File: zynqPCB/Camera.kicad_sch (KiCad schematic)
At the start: 14 parts, among them J4 HDMI_A, U19 PCA9306, U20 xc7z020clg484

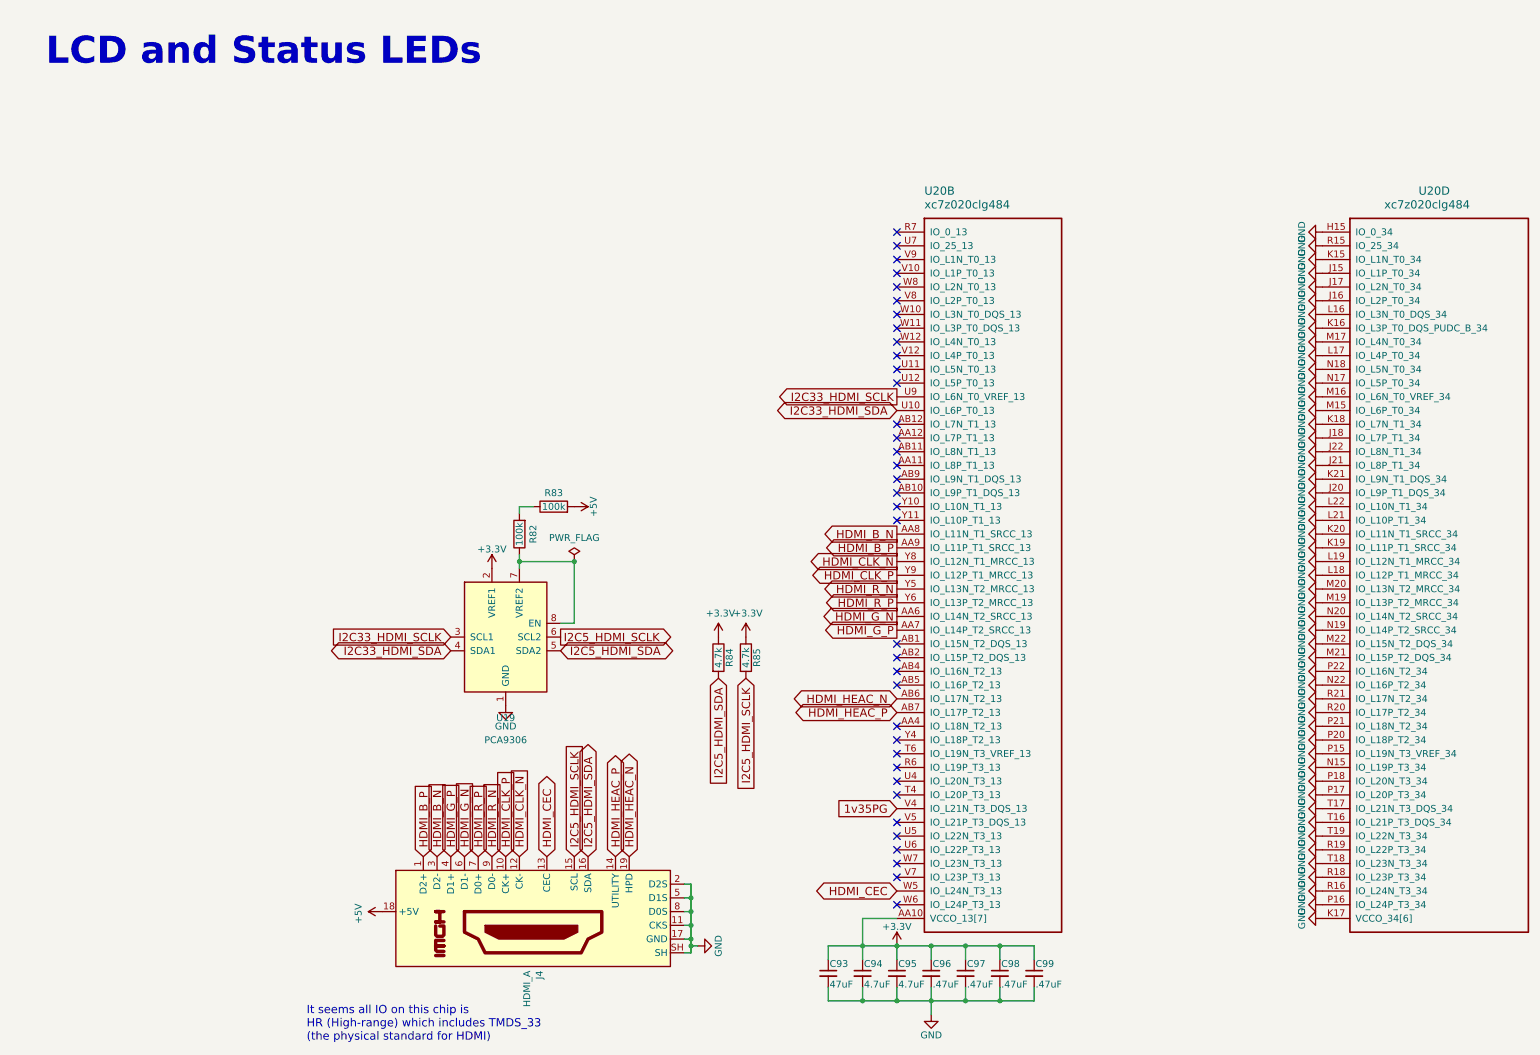
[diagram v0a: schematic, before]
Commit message: Cleared ERC error except the sequencer Part
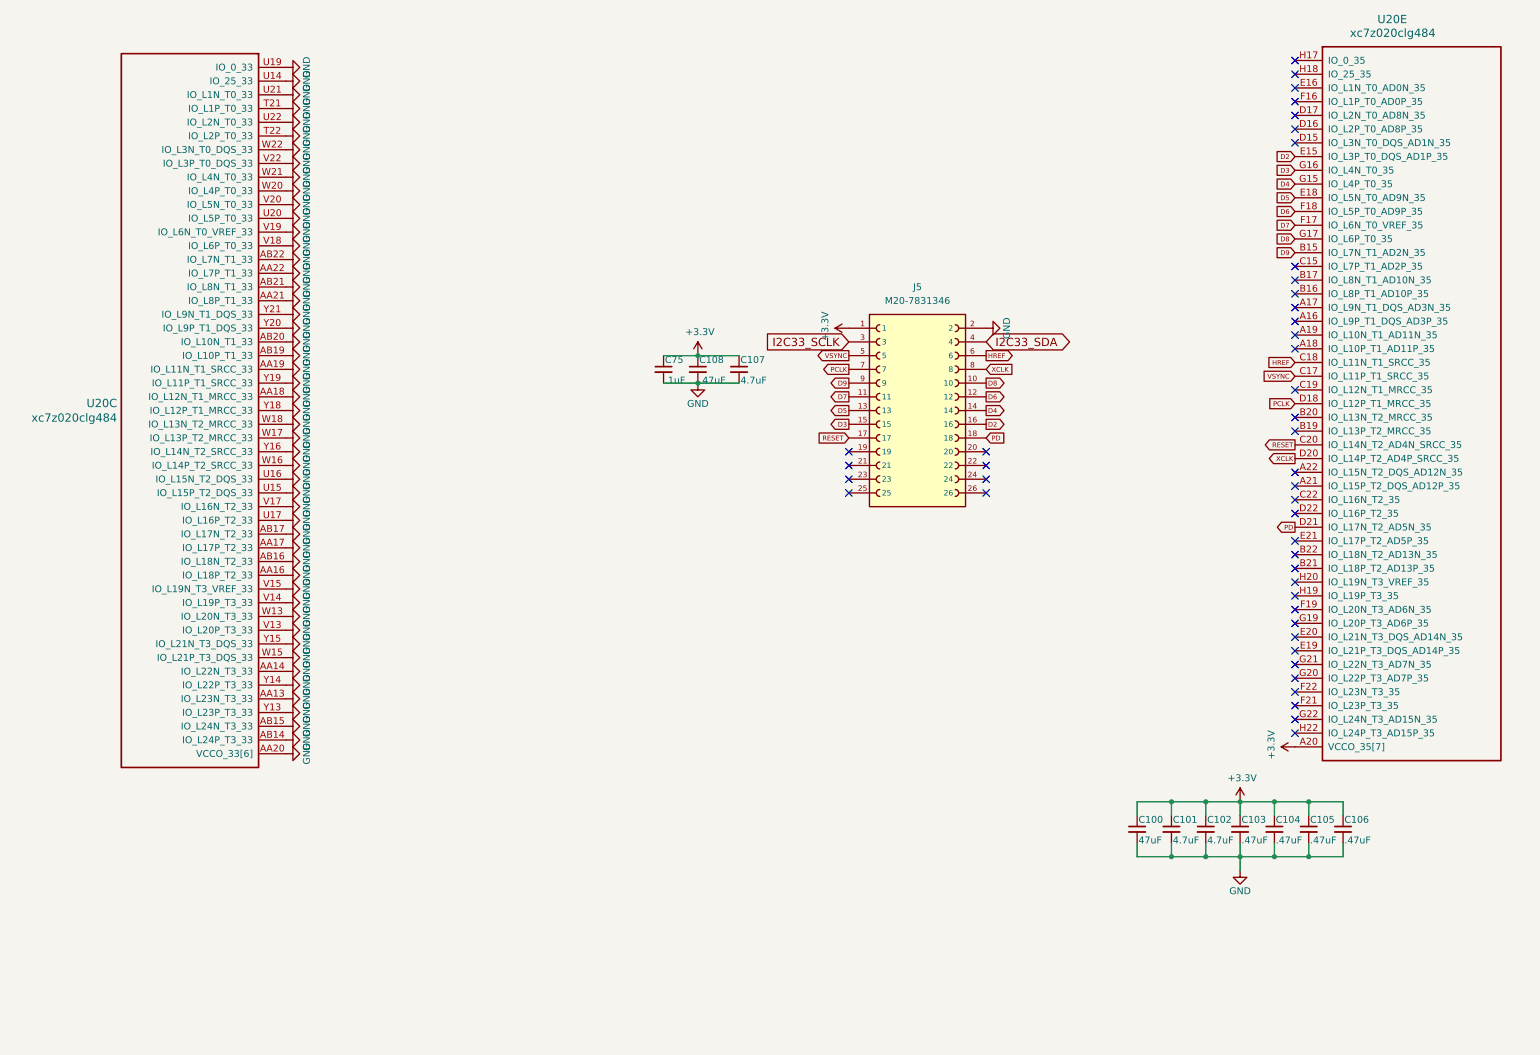
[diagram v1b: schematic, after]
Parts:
- removed C93: 47uF, Capacitor_SMD:C_1210_3225Metric, symbol Device:C_Small
- removed C94, C95: 4.7uF, Capacitor_SMD:C_0402_1005Metric, symbol Device:C_Small
- removed C96, C97, C98, C99: .47uF, Capacitor_SMD:C_0402_1005Metric, symbol Device:C_Small
- removed J4: HDMI_A, DFTcustom:10029449-111RLF, symbol Connector:HDMI_A
- removed R82, R83: 100k, Resistor_SMD:R_0402_1005Metric, symbol Device:R
- removed R84, R85: 4.7k, Resistor_SMD:R_0402_1005Metric, symbol Device:R
- removed U19: PCA9306, Package_SO:SSOP-8_2.95x2.8mm_P0.65mm, symbol Interface:PCA9306
- removed U20: xc7z020clg484, DFTcustom:BGA-484_19.0x19.0mm_Layout22x22_P0.80mm_dia0.40mm, symbol xilinx7:xc7z020clg484
- added C100: 47uF, Capacitor_SMD:C_1210_3225Metric, symbol Device:C_Small
- added C101, C102, C107: 4.7uF, Capacitor_SMD:C_0402_1005Metric, symbol Device:C_Small
- added C103, C104, C105, C106, C108: .47uF, Capacitor_SMD:C_0402_1005Metric, symbol Device:C_Small
- added C75: .1uF, Capacitor_SMD:C_0402_1005Metric, symbol Device:C_Small
- added J5: M20-7831346, M20-7831346:HARWIN_M20-7831346, symbol M20-7831346:M20-7831346
- added U20: xc7z020clg484, DFTcustom:BGA-484_19.0x19.0mm_Layout22x22_P0.80mm_dia0.40mm, symbol xilinx7:xc7z020clg484
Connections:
- net +3.3V: now also C100.1, C101.1, C102.1, C103.1, C104.1, C105.1, C106.1, C107.1, C108.1, C75.1, J5.1, U20.A20 (VCCO_35[7]), U20.C16 (VCCO_35[7]), U20.D19 (VCCO_35[7]), U20.E22 (VCCO_35[7]), U20.F15 (VCCO_35[7]), U20.G18 (VCCO_35[7]), U20.H21 (VCCO_35[7])
- net GND: now also C100.2, C101.2, C102.2, C103.2, C104.2, C105.2, C106.2, C107.2, C108.2, C75.2, J5.2, U20.AA13 (IO_L23N_T3_33), U20.AA14 (IO_L22N_T3_33), U20.AA16 (IO_L18P_T2_33), U20.AA17 (IO_L17P_T2_33), U20.AA18 (IO_L12N_T1_MRCC_33), U20.AA19 (IO_L11N_T1_SRCC_33), U20.AA20 (VCCO_33[6]), U20.AA21 (IO_L8P_T1_33), U20.AA22 (IO_L7P_T1_33), U20.AB13 (VCCO_33[6]), U20.AB14 (IO_L24P_T3_33), U20.AB15 (IO_L24N_T3_33), U20.AB16 (IO_L18N_T2_33), U20.AB17 (IO_L17N_T2_33), U20.AB19 (IO_L10P_T1_33), U20.AB20 (IO_L10N_T1_33), U20.AB21 (IO_L8N_T1_33), U20.AB22 (IO_L7N_T1_33), U20.T21 (IO_L1P_T0_33), U20.T22 (IO_L2P_T0_33), U20.U14 (IO_25_33), U20.U15 (IO_L15P_T2_DQS_33), U20.U16 (IO_L15N_T2_DQS_33), U20.U17 (IO_L16P_T2_33), U20.U18 (VCCO_33[6]), U20.U19 (IO_0_33), U20.U20 (IO_L5P_T0_33), U20.U21 (IO_L1N_T0_33), U20.U22 (IO_L2N_T0_33), U20.V13 (IO_L20P_T3_33), U20.V14 (IO_L19P_T3_33), U20.V15 (IO_L19N_T3_VREF_33), U20.V17 (IO_L16N_T2_33), U20.V18 (IO_L6P_T0_33), U20.V19 (IO_L6N_T0_VREF_33), U20.V20 (IO_L5N_T0_33), U20.V21 (VCCO_33[6]), U20.V22 (IO_L3P_T0_DQS_33), U20.W13 (IO_L20N_T3_33), U20.W14 (VCCO_33[6]), U20.W15 (IO_L21P_T3_DQS_33), U20.W16 (IO_L14P_T2_SRCC_33), U20.W17 (IO_L13P_T2_MRCC_33), U20.W18 (IO_L13N_T2_MRCC_33), U20.W20 (IO_L4P_T0_33), U20.W21 (IO_L4N_T0_33), U20.W22 (IO_L3N_T0_DQS_33), U20.Y13 (IO_L23P_T3_33), U20.Y14 (IO_L22P_T3_33), U20.Y15 (IO_L21N_T3_DQS_33), U20.Y16 (IO_L14N_T2_SRCC_33), U20.Y17 (VCCO_33[6]), U20.Y18 (IO_L12P_T1_MRCC_33), U20.Y19 (IO_L11P_T1_SRCC_33), U20.Y20 (IO_L9P_T1_DQS_33), U20.Y21 (IO_L9N_T1_DQS_33)
- new net D2: J5.16, U20.E15 (IO_L3P_T0_DQS_AD1P_35)
- new net D3: J5.15, U20.G16 (IO_L4N_T0_35)
- new net D4: J5.14, U20.G15 (IO_L4P_T0_35)
- new net D5: J5.13, U20.E18 (IO_L5N_T0_AD9N_35)
- new net D6: J5.12, U20.F18 (IO_L5P_T0_AD9P_35)
- new net D7: J5.11, U20.F17 (IO_L6N_T0_VREF_35)
- new net D8: J5.10, U20.G17 (IO_L6P_T0_35)
- new net D9: J5.9, U20.B15 (IO_L7N_T1_AD2N_35)
- new net HREF: J5.6, U20.C18 (IO_L11N_T1_SRCC_35)
- new net I2C33_SCLK: J5.3
- new net I2C33_SDA: J5.4
- new net PCLK: J5.7, U20.D18 (IO_L12P_T1_MRCC_35)
- new net PD: J5.18, U20.D21 (IO_L17N_T2_AD5N_35)
- new net RESET: J5.17, U20.C20 (IO_L14N_T2_AD4N_SRCC_35)
- new net VSYNC: J5.5, U20.C17 (IO_L11P_T1_SRCC_35)
- new net XCLK: J5.8, U20.D20 (IO_L14P_T2_AD4P_SRCC_35)
- no-connect marks 36 -> 44
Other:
- note removed: "It seems all IO on this chip is HR (High-range) which includes TMDS_33 (the physical standard for HDMI)"
- note removed: "LCD and Status LEDs"

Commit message: Sequencing is taken care
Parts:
- added D1: LED, symbol DFTCustom:LED
- added R4, R5: 4.7k, symbol Device:R
- added R6: 10k, symbol Device:R
- added R9: 330, symbol Device:R
- added SW1: SW_Push, symbol Switch:SW_Push
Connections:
- net +3.3V: now also R4.1, R5.1, R6.1
- net GND: now also D1.2 (A), SW1.2
- net I2C33_SCLK: now also R5.2
- net I2C33_SDA: now also R4.2
- net BTN_CAPTURE: now reaches U20.H17 (IO_0_35)
- net BTN_CAPTURE: now also R6.2, R9.1, SW1.1
- new net: D1.1 (K), R9.2
- no-connect marks 44 -> 43
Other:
- note added: "LED shows the signal FPGA getting"

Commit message: Sanity Checks and added some footprints
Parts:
- removed R4, R5: 4.7k, symbol Device:R
- added R73, R74: 4.7k, Resistor_SMD:R_0402_1005Metric, symbol Device:R
- D1: footprint (none) -> LED_SMD:LED_0603_1608Metric
- J5: footprint M20-7831346:HARWIN_M20-7831346 -> DFTcustom:HARWIN_M20-7831346
- R6: footprint (none) -> Resistor_SMD:R_0402_1005Metric
- R9: footprint (none) -> Resistor_SMD:R_0603_1608Metric
- SW1: footprint (none) -> Button_Switch_SMD:SW_SPST_TL3342
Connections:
- net +3.3V: now also R73.1, R74.1
- net D2: now also U20.G16 (IO_L4N_T0_35); no longer U20.E15 (IO_L3P_T0_DQS_AD1P_35)
- net D3: now also U20.G15 (IO_L4P_T0_35); no longer U20.G16 (IO_L4N_T0_35)
- net D4: now also U20.E18 (IO_L5N_T0_AD9N_35); no longer U20.G15 (IO_L4P_T0_35)
- net D5: now also U20.F18 (IO_L5P_T0_AD9P_35); no longer U20.E18 (IO_L5N_T0_AD9N_35)
- net D6: now also U20.B15 (IO_L7N_T1_AD2N_35); no longer U20.F18 (IO_L5P_T0_AD9P_35)
- net D7: now also U20.C15 (IO_L7P_T1_AD2P_35); no longer U20.F17 (IO_L6N_T0_VREF_35)
- net D8: now also U20.B17 (IO_L8N_T1_AD10N_35); no longer U20.G17 (IO_L6P_T0_35)
- net D9: now also U20.B16 (IO_L8P_T1_AD10P_35); no longer U20.B15 (IO_L7N_T1_AD2N_35)
- net I2C33_SCLK: now also R73.2
- net I2C33_SDA: now also R74.2
- no-connect marks 43 -> 44

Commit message: Ferrite Bead
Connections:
- no-connect marks 44 -> 43
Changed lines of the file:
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@@
-	)
-	(no_connect
-		(at 223.52 60.96)
 	)
 	(no_connect
